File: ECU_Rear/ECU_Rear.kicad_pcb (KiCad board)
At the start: 2 copper layers, 88.9 x 76.2 mm, 21 parts, among them J4 Conn_01x03_Pin, U1 Step_down buck, U2 ESP32-DevKitC, U3 4N25, U4 4N25, U5 4N25

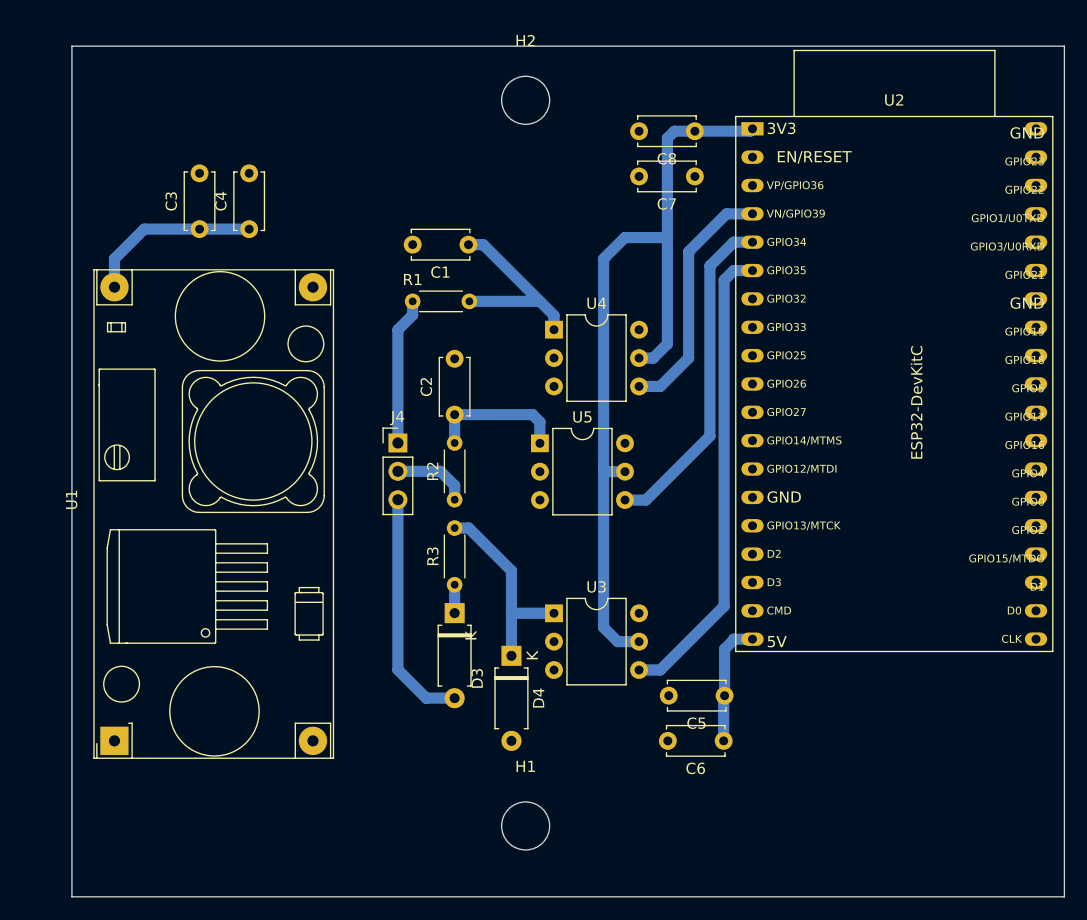
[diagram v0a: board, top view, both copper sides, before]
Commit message: fiz schematic and remake layout
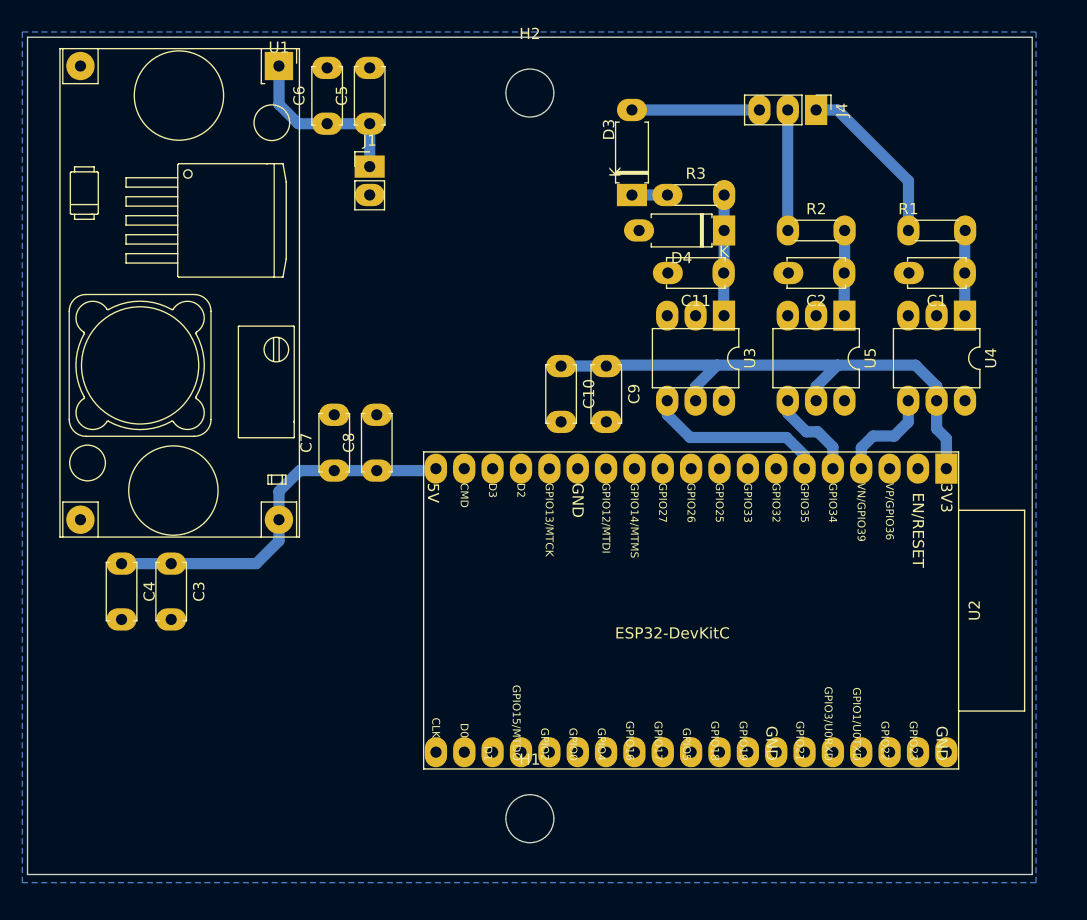
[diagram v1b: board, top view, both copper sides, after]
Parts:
- added C10: 10nF, Capacitor_THT:C_Disc_D5.0mm_W2.5mm_P5.00mm, F.Cu at (137.8, 79.5)
- added C11: 15nF, Capacitor_THT:C_Disc_D5.0mm_W2.5mm_P5.00mm, F.Cu at (152.4, 71.1)
- added C9: 100nF, Capacitor_THT:C_Disc_D5.0mm_W2.5mm_P5.00mm, F.Cu at (141.8, 79.5)
- added J1: Conn_PWR_IN, Connector_PinHeader_2.54mm:PinHeader_1x02_P2.54mm_Vertical, F.Cu at (120.7, 61.6)
- C2: value 100nF -> 15nF
- J4: value Conn_01x03_Pin -> Conn_SENSORS
- R1: value 1,5k -> 200k
- moved C6 65.7 mm to (116.8, 57.7), turned to 90 degrees
- moved U1 62.2 mm to (112.5, 52.6), turned to -90 degrees
- moved C5 60.3 mm to (120.7, 57.7), turned to 90 degrees
- moved J4 47.9 mm to (160.6, 56.5), turned to -90 degrees
- moved R1 44.9 mm to (168.9, 67.3)
- moved C1 44.5 mm to (173.9, 71.1)
- moved D4 42.6 mm to (152.4, 67.3), turned to 180 degrees
- moved C7 41.7 mm to (117.5, 88.8), turned to 90 degrees
- moved C8 41.7 mm to (121.3, 88.8), turned to 90 degrees
- moved D3 40.7 mm to (144.1, 64.1), turned to 90 degrees
- moved R3 39.8 mm to (147.3, 64.1), turned to 0 degrees
- moved R2 38.4 mm to (158.1, 67.3), turned to 0 degrees
- moved C2 37.1 mm to (163.2, 71.1), turned to 180 degrees
- moved U4 36.8 mm to (174.0, 74.9), turned to -90 degrees
- moved U2 35.0 mm to (172.3, 88.6), turned to -90 degrees
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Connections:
- C5 pad 1: +5V -> +12V
- C6 pad 1: +5V -> +12V
- C7 pad 1: +3V3 -> +5V
- C8 pad 1: +3V3 -> +5V
- U2 pad 14: unconnected-(U2-GND-Pad14) -> GND
- U2 pad 32: unconnected-(U2-GND-Pad32) -> GND
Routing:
- net SIGNAL_RPM: track 42.1 -> 16.2 mm
- net +3V3: track 74.6 -> 50.2 mm
- net SIGNAL_INDUCTIVE: track 29.9 -> 8.36 mm
- net +12V: track 0.00 -> 16.2 mm
- net SIGNAL_CAPACITIVE: track 22.1 -> 8.95 mm
- net Net-(C1-Pad1): track 17.9 -> 7.66 mm
- net CONN_RPM: track 21.4 -> 11.4 mm
- net +5V: track 26.9 -> 34.3 mm
- net Net-(D4-K): track 18.1 -> 10.8 mm
- net Net-(C2-Pad1): track 12.4 -> 7.66 mm
- net CONN_INDUCTIVE: track 6.88 -> 10.8 mm
- net CONN_CAPACITIVE: track 13.2 -> 15.3 mm
- net Net-(D3-K): track 2.54 -> 3.17 mm
- added copper zone on B.Cu, net GND
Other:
- board size 88.9 x 76.2 mm -> 90 x 75 mm

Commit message: update ECU Rear
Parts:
- added G***: LOGO, LOGO, B.Cu at (111.1, 111.1)
- C4: footprint Capacitor_THT:C_Disc_D5.0mm_W2.5mm_P5.00mm -> Capacitor_THT:CP_Radial_D6.3mm_P2.50mm
- J1: footprint Connector_PinHeader_2.54mm:PinHeader_1x02_P2.54mm_Vertical -> Connector_JST:JST_XH_B2B-XH-A_1x02_P2.50mm_Vertical
- J4: footprint Connector_PinHeader_2.54mm:PinHeader_1x03_P2.54mm_Vertical -> Connector_JST:JST_XH_B3B-XH-A_1x03_P2.50mm_Vertical
- moved J1 1.91 mm to (120.7, 63.5)
- moved C3 1.91 mm to (104.8, 97.2)
- turned J4 to 180 degrees
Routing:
- net +12V: track 16.2 -> 18.1 mm
